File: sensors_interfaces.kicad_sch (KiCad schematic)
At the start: 30 parts, among them IC601 STK8321, IC602 SP3485EN-L_TR, IC603 WM8782SEDS_RV_C323842, IC604 CS4344-CZZ, IC605 MCP9700AT-E_TT, X601 KF2EDGR-3.81-3P

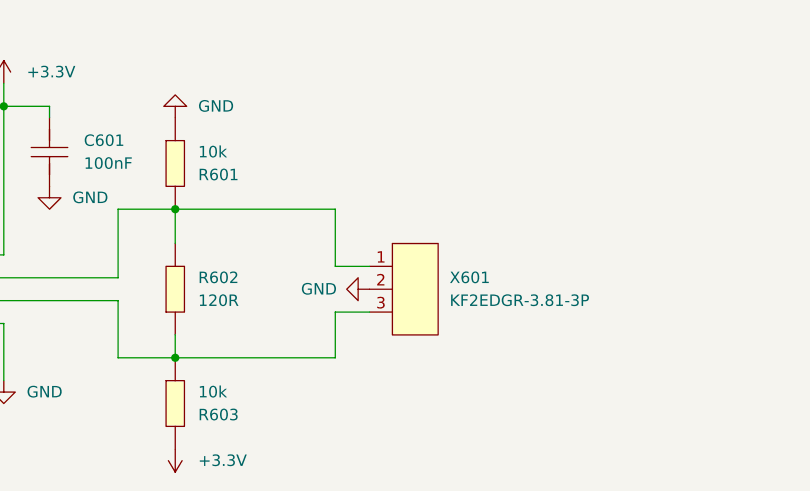
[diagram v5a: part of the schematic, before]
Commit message: move RS485 Connector to connectors page
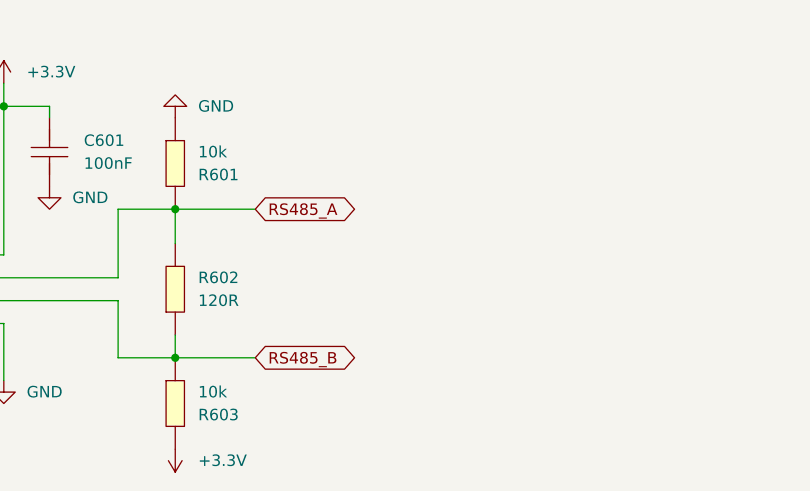
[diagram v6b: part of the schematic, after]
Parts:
- removed X601: KF2EDGR-3.81-3P, CONN-TH_3P-P3.81_KF2EDGR-3.81-3P, symbol eduboardv2:KF2EDGR-3.81-3P
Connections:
- net RS485_B: now reaches IC602.6 (A), R602.1, R603.1
- net RS485_A: now reaches IC602.7 (B), R601.2, R602.2
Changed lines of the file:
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@@
-    (stroke (width 0) (type default) (color 0 0 0 0))
-  )
-  (wire (pts (xy 93.98 172.72) (xy 93.98 166.37))
     (stroke (width 0) (type default) (color 0 0 0 0))
   )
@@
     (stroke (width 0) (type default) (color 0 0 0 0))
   )
-  (wire (pts (xy 97.79 177.8) (xy 93.98 177.8))
-    (stroke (width 0) (type default) (color 0 0 0 0))
-  )
   (wire (pts (xy 69.85 182.88) (xy 76.2 182.88))
     (stroke (width 0) (type default) (color 0 0 0 0))
   )
-  (wire (pts (xy 93.98 177.8) (xy 93.98 182.88))
-    (stroke (width 0) (type default) (color 0 0 0 0))
-  )
   (wire (pts (xy 43.18 115.57) (xy 43.18 124.46))
     (stroke (width 0) (type default) (color 0 0 0 0))
@@
     (stroke (width 0) (type default) (color 0 0 0 0))
   )
-  (wire (pts (xy 76.2 182.88) (xy 93.98 182.88))
-    (stroke (width 0) (type default) (color 0 0 0 0))
-  )
   (wire (pts (xy 200.66 71.12) (xy 200.66 92.71))
     (stroke (width 0) (type default) (color 0 0 0 0))
@@
     (stroke (width 0) (type default) (color 0 0 0 0))
   )
-  (wire (pts (xy 93.98 166.37) (xy 76.2 166.37))
-    (stroke (width 0) (type default) (color 0 0 0 0))
-  )
   (wire (pts (xy 74.93 97.79) (xy 63.5 97.79))
     (stroke (width 0) (type default) (color 0 0 0 0))
@@
     (stroke (width 0) (type default) (color 0 0 0 0))
   )
-  (wire (pts (xy 97.79 172.72) (xy 93.98 172.72))
-    (stroke (width 0) (type default) (color 0 0 0 0))
-  )
   (wire (pts (xy 33.02 179.07) (xy 35.56 179.07))
     (stroke (width 0) (type default) (color 0 0 0 0))
@@
     (stroke (width 0) (type default) (color 0 0 0 0))
   )
+  (wire (pts (xy 76.2 166.37) (xy 85.09 166.37))
+    (stroke (width 0) (type default) (color 0 0 0 0))
+  )
   (wire (pts (xy 167.64 92.71) (xy 171.45 92.71))
     (stroke (width 0) (type default) (color 0 0 0 0))
@@
   )
   (wire (pts (xy 167.64 90.17) (xy 171.45 90.17))
+    (stroke (width 0) (type default) (color 0 0 0 0))
+  )
+  (wire (pts (xy 76.2 182.88) (xy 85.09 182.88))
     (stroke (width 0) (type default) (color 0 0 0 0))
   )
@@
     )
   )
+  (global_label "RS485_A" (shape bidirectional) (at 85.09 166.37 0) (fields_autoplaced)
+    (effects (font (size 1.27 1.27)) (justify left))
+    (property "Intersheet References" "${INTERSHEET_REFS}" (id 0) (at 95.6674 166.4494 0)
+      (effects (font (size 1.27 1.27)) (justify left) hide)
+    )
+  )
   (global_label "UART_RS485_RX" (shape output) (at 33.02 171.45 180) (fields_autoplaced)
     (effects (font (size 1.27 1.27)) (justify right))
@@
     (property "Intersheet References" "${INTERSHEET_REFS}" (id 0) (at 155.2483 92.6306 0)
       (effects (font (size 1.27 1.27)) (justify right) hide)
+    )
+  )
+  (global_label "RS485_B" (shape bidirectional) (at 85.09 182.88 0) (fields_autoplaced)
+    (effects (font (size 1.27 1.27)) (justify left))
+    (property "Intersheet References" "${INTERSHEET_REFS}" (id 0) (at 95.8488 182.9594 0)
+      (effects (font (size 1.27 1.27)) (justify left) hide)
     )
   )
@@
     (pin "1")
   )
-  (symbol (lib_id "eduboardv2:KF2EDGR-3.81-3P") (at 102.87 175.26 0) (unit 1)
-    (in_bom yes) (on_board yes) (fields_autoplaced)
-    (property "Reference" "X601" (id 0) (at 106.68 173.9899 0)
-      (effects (font (size 1.27 1.27)) (justify left))
-    )
-    (property "Value" "KF2EDGR-3.81-3P" (id 1) (at 106.68 176.5299 0)
-      (effects (font (size 1.27 1.27)) (justify left))
-    )
-    (property "Footprint" "CONN-TH_3P-P3.81_KF2EDGR-3.81-3P" (id 2) (at 102.87 185.42 0)
-      (effects (font (size 1.27 1.27)) hide)
-    )
-    (property "Datasheet" "https://lcsc.com/product-detail/Pluggable-System-Terminal-Block_Cixi-Kefa-Elec-KF2EDGR-3-81-3P_C441183.html" (id 3) (at 102.87 190.5 0)
-      (effects (font (size 1.27 1.27)) hide)
-    )
-    (property "Manufacturer" "Cixi Kefa Elec" (id 4) (at 102.87 193.04 0)
-      (effects (font (size 1.27 1.27)) hide)
-    )
-    (property "LCSC Part" "C441183" (id 5) (at 102.87 195.58 0)
-      (effects (font (size 1.27 1.27)) hide)
-    )
-    (property "JLC Part" "Extended Part" (id 6) (at 102.87 198.12 0)
-      (effects (font (size 1.27 1.27)) hide)
-    )
-    (property "MPN" "KF2EDGR-3.81-3P" (id 7) (at 102.87 182.88 0)
-      (effects (font (size 1.27 1.27)) hide)
-    )
-    (pin "1")
-    (pin "2")
-    (pin "3")
-  )
   (symbol (lib_name "GND_25") (lib_id "eduboardv2:GND") (at 25.4 139.7 0) (unit 1)
     (in_bom yes) (on_board yes) (fields_autoplaced)
@@
     (pin "2")
   )
-  (symbol (lib_name "GND_8") (lib_id "eduboardv2:GND") (at 97.79 175.26 270) (unit 1)
-    (in_bom yes) (on_board yes)
-    (property "Reference" "#PWR0606" (id 0) (at 91.44 175.26 0)
-      (effects (font (size 1.27 1.27)) hide)
-    )
-    (property "Value" "GND" (id 1) (at 90.17 175.26 90)
-      (effects (font (size 1.27 1.27)) (justify left))
-    )
-    (property "Footprint" "" (id 2) (at 97.79 175.26 0)
-      (effects (font (size 1.27 1.27)) hide)
-    )
-    (property "Datasheet" "" (id 3) (at 97.79 175.26 0)
-      (effects (font (size 1.27 1.27)) hide)
-    )
-    (pin "1")
-  )
   (symbol (lib_name "CL10A106MA8NRNC_1") (lib_id "eduboardv2:CL10A106MA8NRNC") (at 166.37 109.22 90) (unit 1)

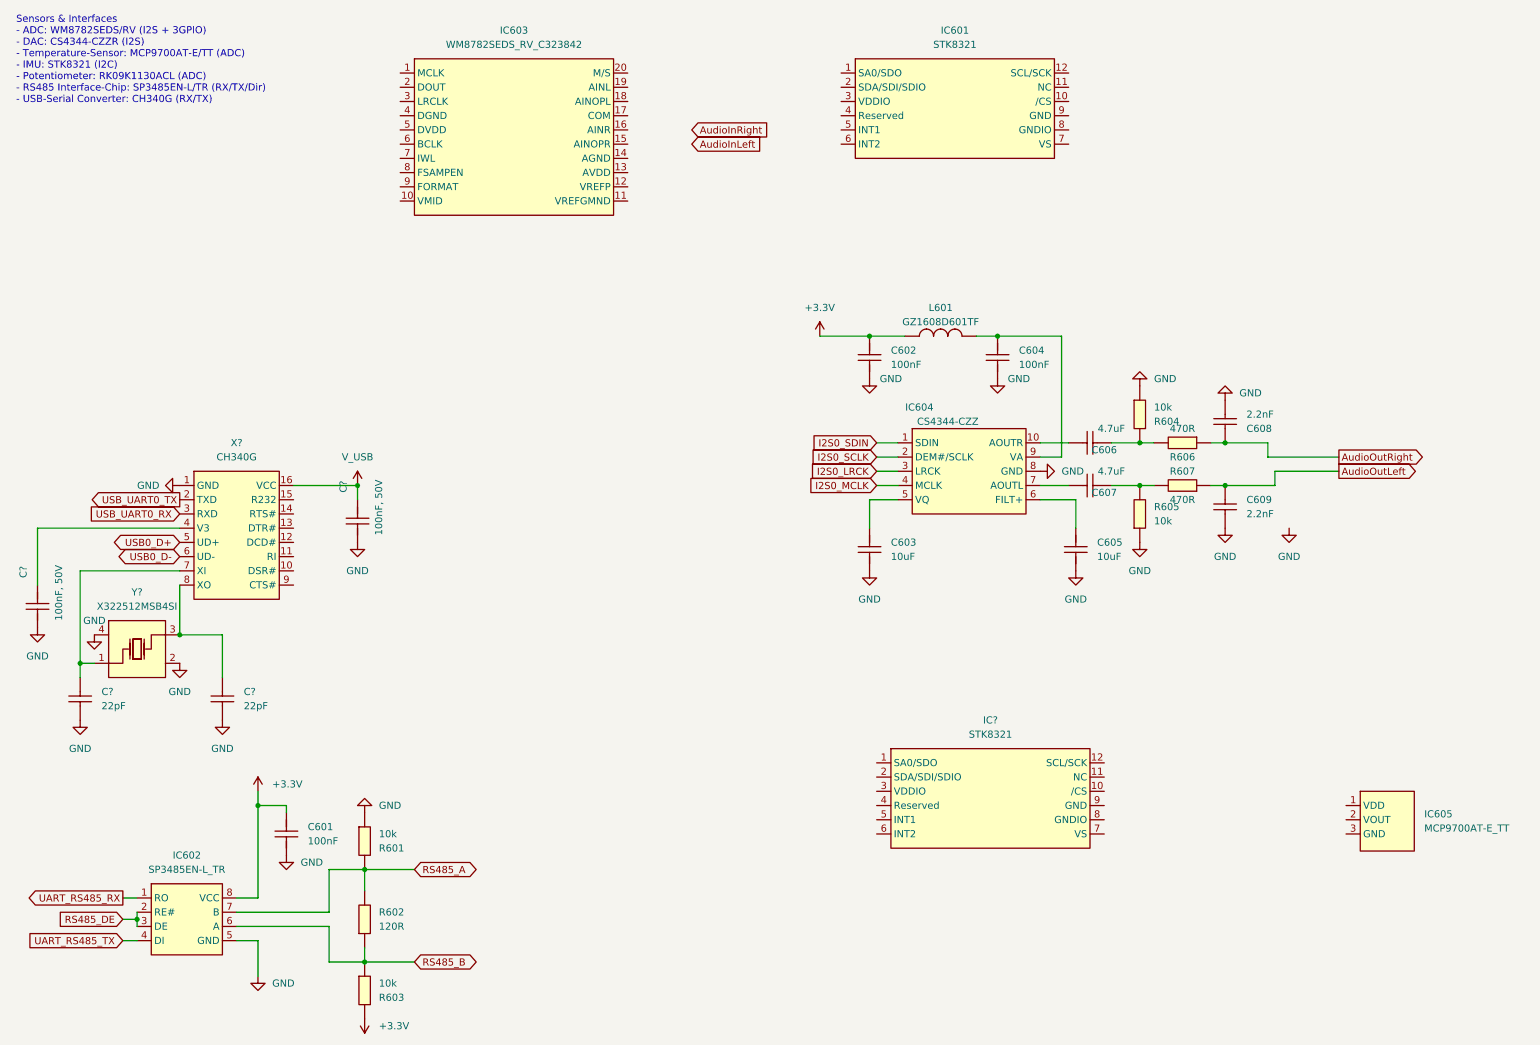
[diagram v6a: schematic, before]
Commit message: reassign symbol references after page movements. Place in pcb
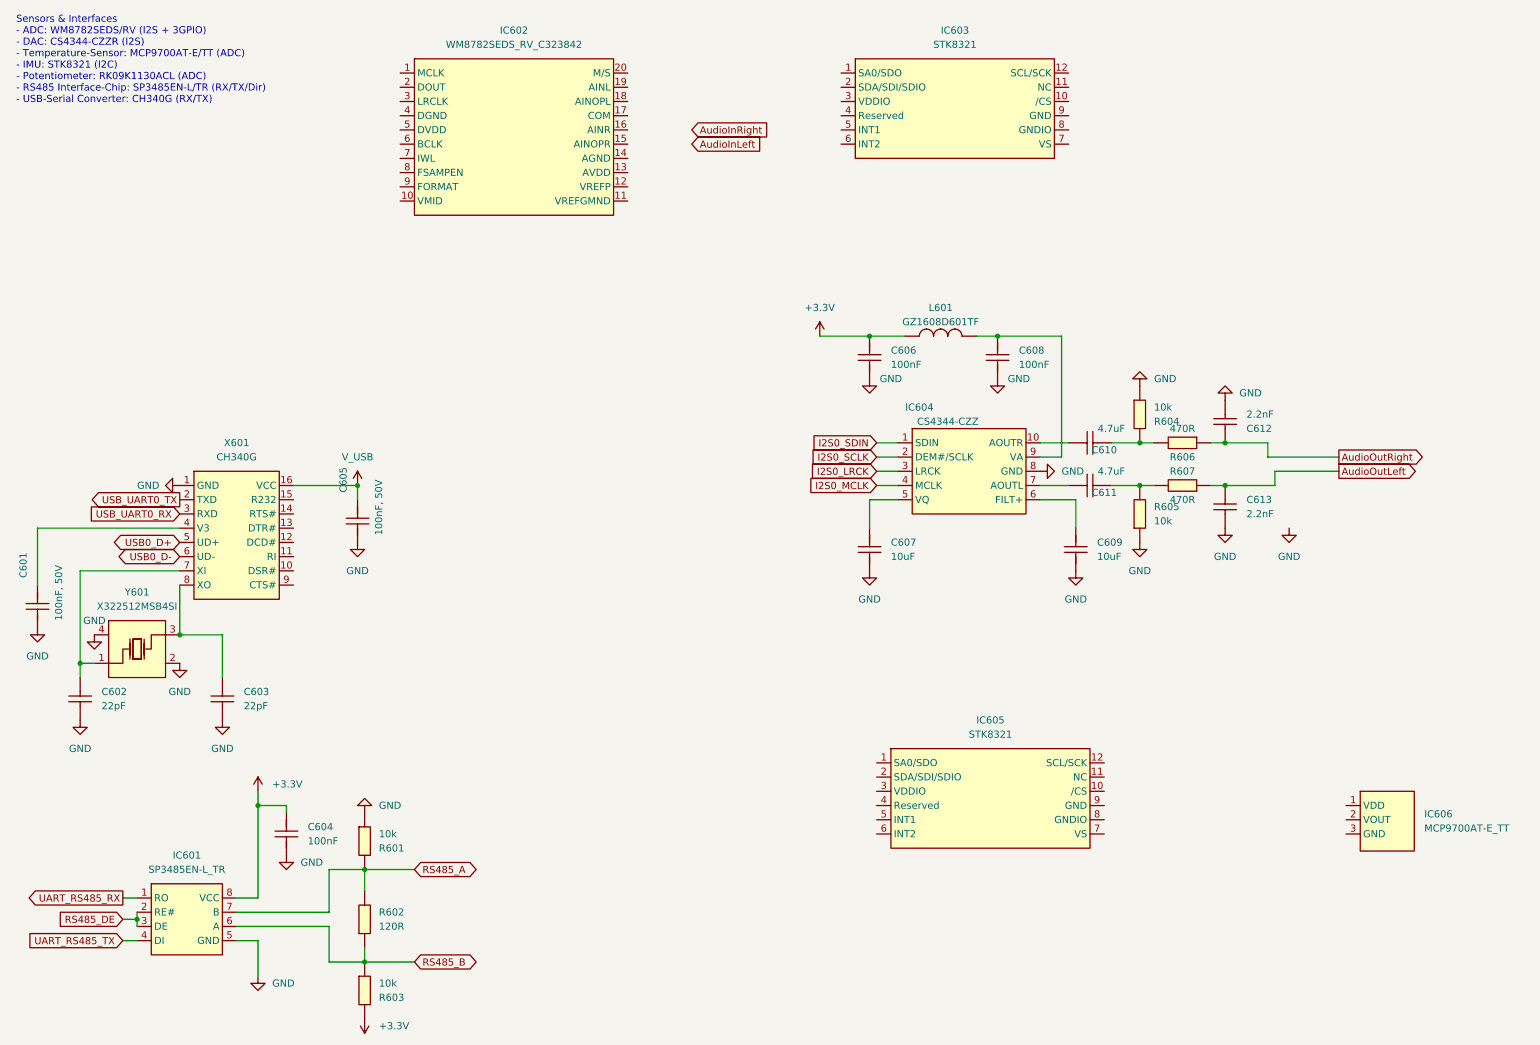
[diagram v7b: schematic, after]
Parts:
- C601, C602, C603, C605: renamed from C?; footprint C0402 -> eduboardv2:C0402
- C604: renamed from C601; footprint C0402 -> eduboardv2:C0402
- C606: renamed from C602; footprint C0402 -> eduboardv2:C0402
- C607: renamed from C603; footprint C0603 -> eduboardv2:C0603
- C608: renamed from C604; footprint C0402 -> eduboardv2:C0402
- C609: renamed from C605; footprint C0603 -> eduboardv2:C0603
- C610: renamed from C606; footprint C0603 -> eduboardv2:C0603
- C611: renamed from C607; footprint C0603 -> eduboardv2:C0603
- C612: renamed from C608; footprint C0402 -> eduboardv2:C0402
- C613: renamed from C609; footprint C0402 -> eduboardv2:C0402
- IC601: renamed from IC602; footprint SOIC-8_L5.0-W4.0-P1.27-LS6.0-BL -> eduboardv2:SOIC-8_L5.0-W4.0-P1.27-LS6.0-BL
- IC602: renamed from IC603; footprint SSOP-20_L7.5-W5.2-P0.65-LS8.0-BL -> eduboardv2:SSOP-20_L7.5-W5.2-P0.65-LS8.0-BL
- IC603: renamed from IC601; footprint LGA-12_L2.0-W2.0-P0.50-TR -> eduboardv2:LGA-12_L2.0-W2.0-P0.50-TR
- IC604: footprint TSSOP-10_L3.0-W3.0-P0.50-LS4.9-BL -> eduboardv2:TSSOP-10_L3.0-W3.0-P0.50-LS4.9-BL
- IC605: renamed from IC?; footprint LGA-12_L2.0-W2.0-P0.50-TR -> eduboardv2:LGA-12_L2.0-W2.0-P0.50-TR
- IC606: renamed from IC605; footprint SOT-23-3_L2.9-W1.3-P1.90-LS2.4-BR -> eduboardv2:SOT-23-3_L2.9-W1.3-P1.90-LS2.4-BR
- L601: footprint L0603 -> eduboardv2:L0603
- R601, R602, R603, R604, R605, R606, R607: footprint R0402 -> eduboardv2:R0402
- X601: renamed from X?; footprint SOIC-16_L9.9-W3.9-P1.27-LS6.0-BL -> eduboardv2:SOIC-16_L9.9-W3.9-P1.27-LS6.0-BL
- Y601: renamed from Y?; footprint OSC-SMD_4P-L3.2-W2.5-BL -> eduboardv2:OSC-SMD_4P-L3.2-W2.5-BL

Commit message: fix power symbol problem.
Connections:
- net GND: now reaches C609.1
- net GND: now also C601.1, C602.1, C603.1, C604.1, C605.1, C606.1, C607.1, C608.1, C612.1, C613.1, IC601.5 (GND), IC604.8 (GND), R601.1, R604.1, R605.1, X601.1 (GND), Y601.2 (GND), Y601.4 (GND)
- net +3.3V: now reaches C606.2, L601.1
- net +3.3V: now also C604.2, IC601.8 (VCC), R603.2
- net V_USB: now reaches C605.2, X601.16 (VCC)
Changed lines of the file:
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@@
     (pin "1")
   )
-  (symbol (lib_name "GND_4") (lib_id "eduboardv2:GND") (at 203.2 113.03 0) (unit 1)
+  (symbol (lib_id "eduboardv2:GND") (at 203.2 113.03 0) (unit 1)
     (in_bom yes) (on_board yes) (fields_autoplaced)
     (property "Reference" "#PWR0619" (id 0) (at 203.2 119.38 0)
@@
     (pin "1")
   )
-  (symbol (lib_name "GND_9") (lib_id "eduboardv2:GND") (at 76.2 156.21 180) (unit 1)
+  (symbol (lib_id "eduboardv2:GND") (at 76.2 156.21 180) (unit 1)
     (in_bom yes) (on_board yes) (fields_autoplaced)
     (property "Reference" "#PWR0612" (id 0) (at 76.2 149.86 0)
@@
     (pin "2")
   )
-  (symbol (lib_name "GND_12") (lib_id "eduboardv2:GND") (at 241.3 105.41 0) (unit 1)
+  (symbol (lib_id "eduboardv2:GND") (at 241.3 105.41 0) (unit 1)
     (in_bom yes) (on_board yes) (fields_autoplaced)
     (property "Reference" "#PWR0624" (id 0) (at 241.3 111.76 0)
@@
     (pin "2")
   )
-  (symbol (lib_name "GND_13") (lib_id "eduboardv2:GND") (at 214.63 80.01 180) (unit 1)
+  (symbol (lib_id "eduboardv2:GND") (at 214.63 80.01 180) (unit 1)
     (in_bom yes) (on_board yes) (fields_autoplaced)
     (property "Reference" "#PWR0620" (id 0) (at 214.63 73.66 0)
@@
     (pin "1")
   )
-  (symbol (lib_name "GND_25") (lib_id "eduboardv2:GND") (at 25.4 139.7 0) (unit 1)
+  (symbol (lib_id "eduboardv2:GND") (at 25.4 139.7 0) (unit 1)
     (in_bom yes) (on_board yes) (fields_autoplaced)
     (property "Reference" "#PWR0602" (id 0) (at 25.4 146.05 0)
@@
     (pin "1")
   )
-  (symbol (lib_name "GND_3") (lib_id "eduboardv2:GND") (at 166.37 78.74 0) (unit 1)
+  (symbol (lib_id "eduboardv2:GND") (at 166.37 78.74 0) (unit 1)
     (in_bom yes) (on_board yes)
     (property "Reference" "#PWR0615" (id 0) (at 166.37 85.09 0)
@@
     (pin "1")
   )
-  (symbol (lib_name "GND_10") (lib_id "eduboardv2:GND") (at 57.15 185.42 0) (unit 1)
+  (symbol (lib_id "eduboardv2:GND") (at 57.15 185.42 0) (unit 1)
     (in_bom yes) (on_board yes) (fields_autoplaced)
     (property "Reference" "#PWR0608" (id 0) (at 57.15 191.77 0)
@@
     (pin "2")
   )
-  (symbol (lib_name "GND_22") (lib_id "eduboardv2:GND") (at 50.8 139.7 0) (unit 1)
+  (symbol (lib_id "eduboardv2:GND") (at 50.8 139.7 0) (unit 1)
     (in_bom yes) (on_board yes) (fields_autoplaced)
     (property "Reference" "#PWR0606" (id 0) (at 50.8 146.05 0)
@@
     (pin "1")
   )
-  (symbol (lib_name "GND_7") (lib_id "eduboardv2:GND") (at 74.93 107.95 0) (unit 1)
+  (symbol (lib_id "eduboardv2:GND") (at 74.93 107.95 0) (unit 1)
     (in_bom yes) (on_board yes) (fields_autoplaced)
     (property "Reference" "#PWR0611" (id 0) (at 74.93 114.3 0)
@@
     (pin "2")
   )
-  (symbol (lib_name "GND_24") (lib_id "eduboardv2:GND") (at 27.94 124.46 0) (unit 1)
+  (symbol (lib_id "eduboardv2:GND") (at 27.94 124.46 0) (unit 1)
     (in_bom yes) (on_board yes)
     (property "Reference" "#PWR0603" (id 0) (at 27.94 130.81 0)
@@
     (pin "2")
   )
-  (symbol (lib_name "GND_2") (lib_id "eduboardv2:GND") (at 196.85 95.25 90) (unit 1)
+  (symbol (lib_id "eduboardv2:GND") (at 196.85 95.25 90) (unit 1)
     (in_bom yes) (on_board yes) (fields_autoplaced)
     (property "Reference" "#PWR0618" (id 0) (at 203.2 95.25 0)
@@
     (pin "1")
   )
-  (symbol (lib_name "GND_11") (lib_id "eduboardv2:GND") (at 229.87 82.55 180) (unit 1)
+  (symbol (lib_id "eduboardv2:GND") (at 229.87 82.55 180) (unit 1)
     (in_bom yes) (on_board yes) (fields_autoplaced)
     (property "Reference" "#PWR0622" (id 0) (at 229.87 76.2 0)
@@
     (pin "1")
   )
-  (symbol (lib_name "GND_23") (lib_id "eduboardv2:GND") (at 43.18 129.54 0) (unit 1)
+  (symbol (lib_id "eduboardv2:GND") (at 43.18 129.54 0) (unit 1)
     (in_bom yes) (on_board yes) (fields_autoplaced)
     (property "Reference" "#PWR0605" (id 0) (at 43.18 135.89 0)
@@
     (pin "1")
   )
-  (symbol (lib_name "V_USB_2") (lib_id "eduboardv2:V_USB") (at 74.93 97.79 0) (unit 1)
+  (symbol (lib_id "eduboardv2:V_USB") (at 74.93 97.79 0) (unit 1)
     (in_bom yes) (on_board yes) (fields_autoplaced)
     (property "Reference" "#PWR0610" (id 0) (at 74.93 101.6 0)
@@
     (pin "2")
   )
-  (symbol (lib_name "GND_21") (lib_id "eduboardv2:GND") (at 43.18 97.79 270) (mirror x) (unit 1)
+  (symbol (lib_id "eduboardv2:GND") (at 43.18 97.79 270) (mirror x) (unit 1)
     (in_bom yes) (on_board yes)
     (property "Reference" "#PWR0604" (id 0) (at 36.83 97.79 0)
@@
     (pin "1")
   )
-  (symbol (lib_name "GND_6") (lib_id "eduboardv2:GND") (at 189.23 78.74 0) (unit 1)
+  (symbol (lib_id "eduboardv2:GND") (at 189.23 78.74 0) (unit 1)
     (in_bom yes) (on_board yes)
     (property "Reference" "#PWR0617" (id 0) (at 189.23 85.09 0)
@@
     (pin "1")
   )
-  (symbol (lib_name "GND_1") (lib_id "eduboardv2:GND") (at 166.37 113.03 0) (unit 1)
+  (symbol (lib_id "eduboardv2:GND") (at 166.37 113.03 0) (unit 1)
     (in_bom yes) (on_board yes) (fields_autoplaced)
     (property "Reference" "#PWR0616" (id 0) (at 166.37 119.38 0)
@@
     (pin "2")
   )
-  (symbol (lib_name "GND_5") (lib_id "eduboardv2:GND") (at 214.63 107.95 0) (unit 1)
+  (symbol (lib_id "eduboardv2:GND") (at 214.63 107.95 0) (unit 1)
     (in_bom yes) (on_board yes) (fields_autoplaced)
     (property "Reference" "#PWR0621" (id 0) (at 214.63 114.3 0)
@@
     (pin "1")
   )
-  (symbol (lib_name "GND_20") (lib_id "eduboardv2:GND") (at 17.78 123.19 0) (unit 1)
+  (symbol (lib_id "eduboardv2:GND") (at 17.78 123.19 0) (unit 1)
     (in_bom yes) (on_board yes) (fields_autoplaced)
     (property "Reference" "#PWR0601" (id 0) (at 17.78 129.54 0)
@@
     (pin "2")
   )
-  (symbol (lib_name "+3.3V_1") (lib_id "eduboardv2:+3.3V") (at 157.48 71.12 0) (unit 1)
+  (symbol (lib_id "eduboardv2:+3.3V") (at 157.48 71.12 0) (unit 1)
     (in_bom yes) (on_board yes) (fields_autoplaced)
     (property "Reference" "#PWR0614" (id 0) (at 157.48 74.93 0)
@@
     (pin "9")
   )
-  (symbol (lib_name "GND_7") (lib_id "eduboardv2:GND") (at 62.23 163.83 0) (unit 1)
+  (symbol (lib_id "eduboardv2:GND") (at 62.23 163.83 0) (unit 1)
     (in_bom yes) (on_board yes) (fields_autoplaced)
     (property "Reference" "#PWR0609" (id 0) (at 62.23 170.18 0)
